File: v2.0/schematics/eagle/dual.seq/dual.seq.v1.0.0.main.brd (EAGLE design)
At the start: 86 x 80 mm, 75 parts, among them IC1 LM324N, IC2 PIC18F2431DIP, IC3 TL084P, IC4 LM324N, IC5 TL082P, J1 RST1, J2 RST2, J3 DIR1, J4 DIR2, J5 CK1, J6 CK2, Q1 20MHz

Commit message: Initial board layout for dual seq main
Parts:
- R1, R10, R11, R12, R13, R14, R15, R16, R17, R18, R19, R2, R20, R21, R22, R23, R24, R25, R26, R27, R28, R29, R3, R30, R31, R32, R33, R4, R5, R6, R7, R8, R9: device _common:0309/10 -> _common:0207/7
- moved LED2 197.7 mm to (88.9, 2.54), turned to 180 degrees
- moved R16 173.8 mm to (85.1, 29.2), turned to 90 degrees
- moved R10 171.5 mm to (87.6, 47.0)
- moved R15 159.1 mm to (82.5, 29.2), turned to 90 degrees
- moved R22 159.1 mm to (69.8, 35.6), turned to 270 degrees
- moved R4 156.0 mm to (64.8, 35.6), turned to 90 degrees
- moved LED1 152.9 mm to (95.9, 2.54), turned to 180 degrees
- moved D3 151.3 mm to (87.6, 44.5)
- moved R3 151.0 mm to (72.4, 35.6), turned to 270 degrees
- moved D5 150.3 mm to (62.2, 15.2), turned to 270 degrees
- moved IC1 149.8 mm to (64.8, 25.4), turned to 180 degrees
- moved R2 141.4 mm to (69.8, 15.2), turned to 270 degrees
- moved R9 137.7 mm to (57.1, 15.2), turned to 270 degrees
- moved D4 133.1 mm to (54.6, 15.2), turned to 270 degrees
- moved R20 132.6 mm to (67.3, 35.6), turned to 270 degrees
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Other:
- board size 86 x 80 mm -> 98.7 x 62.2 mm

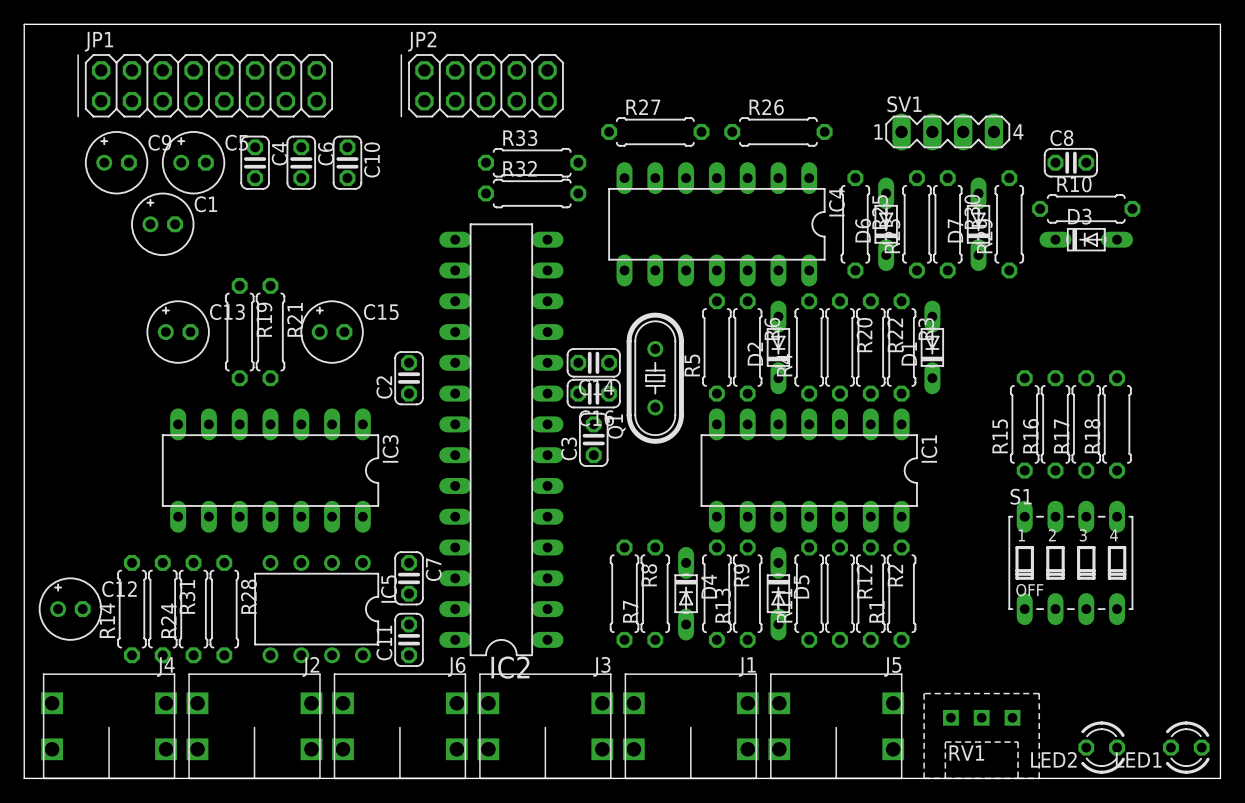
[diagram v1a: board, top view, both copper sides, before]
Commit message: Inital routing for main pnl (too many vias)
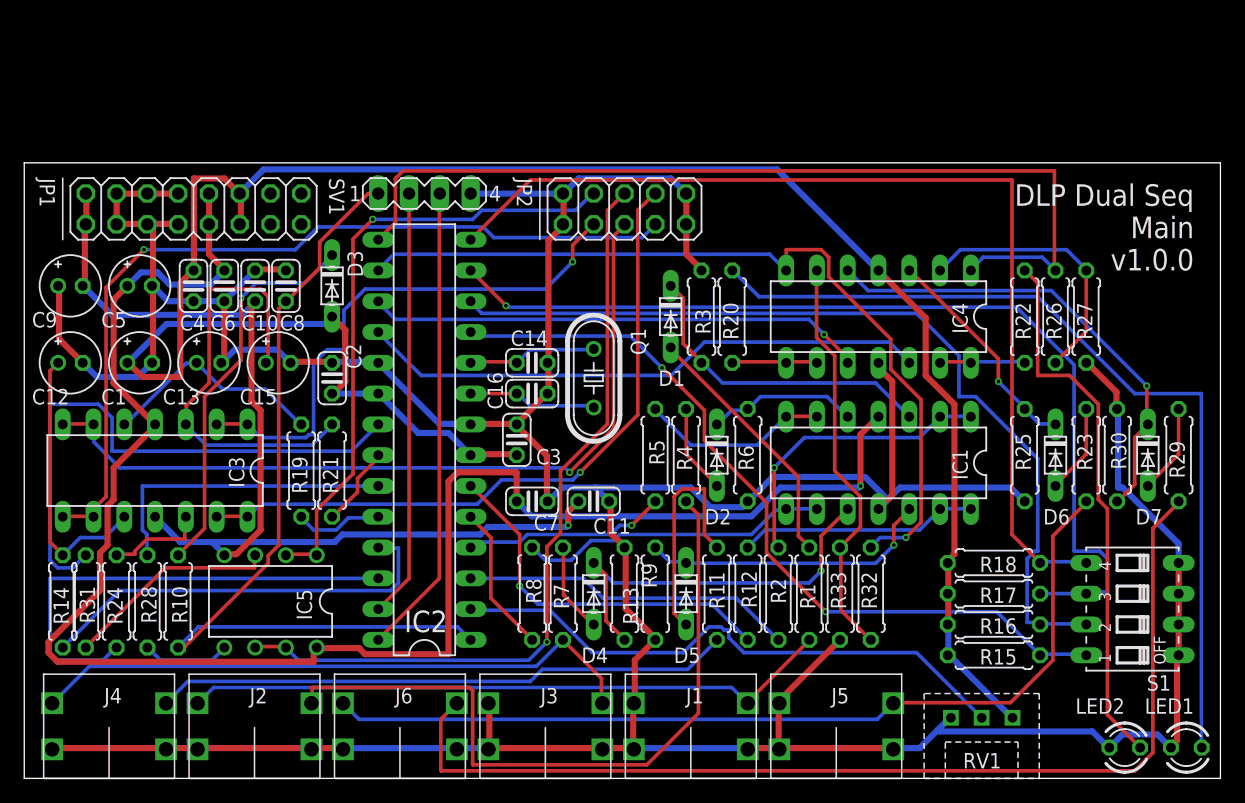
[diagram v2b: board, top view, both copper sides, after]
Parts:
- moved R10 81.6 mm to (12.7, 14.6), turned to 270 degrees
- moved C8 65.6 mm to (21.6, 40.6), turned to 270 degrees
- moved D3 62.3 mm to (25.4, 40.6), turned to 270 degrees
- moved R33 43.7 mm to (67.3, 15.2), turned to 90 degrees
- moved SV1 43.5 mm to (33.0, 48.3)
- moved R32 43.3 mm to (69.8, 15.2), turned to 90 degrees
- moved R27 38.7 mm to (87.6, 38.1), turned to 90 degrees
- moved R26 27.5 mm to (85.1, 38.1), turned to 90 degrees
- moved D6 23.6 mm to (85.1, 26.7), turned to 270 degrees
- moved D7 23.6 mm to (92.7, 26.7), turned to 270 degrees
- moved R23 23.6 mm to (87.6, 26.7)
- moved R25 23.6 mm to (82.5, 26.7), turned to 90 degrees
- moved R29 23.6 mm to (95.2, 26.7)
- moved R30 23.6 mm to (90.2, 26.7)
- moved D1 21.7 mm to (53.3, 38.1), turned to 270 degrees
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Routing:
- net 0V: track 0.00 -> 367.8 mm
- net +5V: track 0.00 -> 171.0 mm
- net +12V: track 0.00 -> 145.5 mm, vias 0 -> 1
- net N$41: track 0.00 -> 87.1 mm
- net -12V: track 0.00 -> 85.9 mm, vias 0 -> 1
- net N$43: track 0.00 -> 83.2 mm
- net N$29: track 0.00 -> 79.9 mm, vias 0 -> 1
- net N$19: track 0.00 -> 76.4 mm
- net N$30: track 0.00 -> 75.4 mm
- net N$28: track 0.00 -> 73.4 mm
- net N$38: track 0.00 -> 72.1 mm
- net VPP: track 0.00 -> 70.4 mm
- net N$21: track 0.00 -> 70.3 mm, vias 0 -> 1
- net N$CV3: track 0.00 -> 70.2 mm, vias 0 -> 1
- net N$CV2: track 0.00 -> 66.6 mm, vias 0 -> 1
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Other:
- board size 98.7 x 62.2 mm -> 98.7 x 50.8 mm
- board text added: "DLP Dual Seq Main v1.0.0"

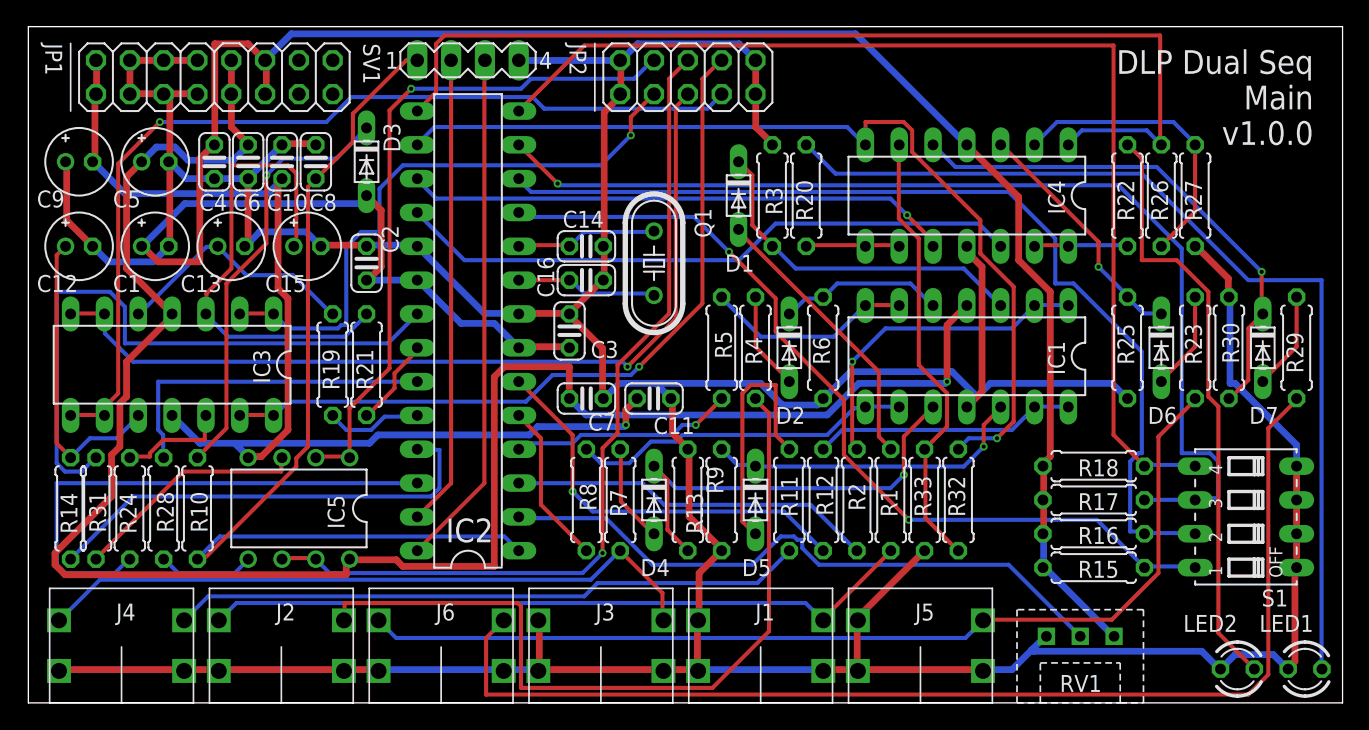
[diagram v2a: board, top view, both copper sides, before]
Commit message: Upated layout and routing for dual.seq main board
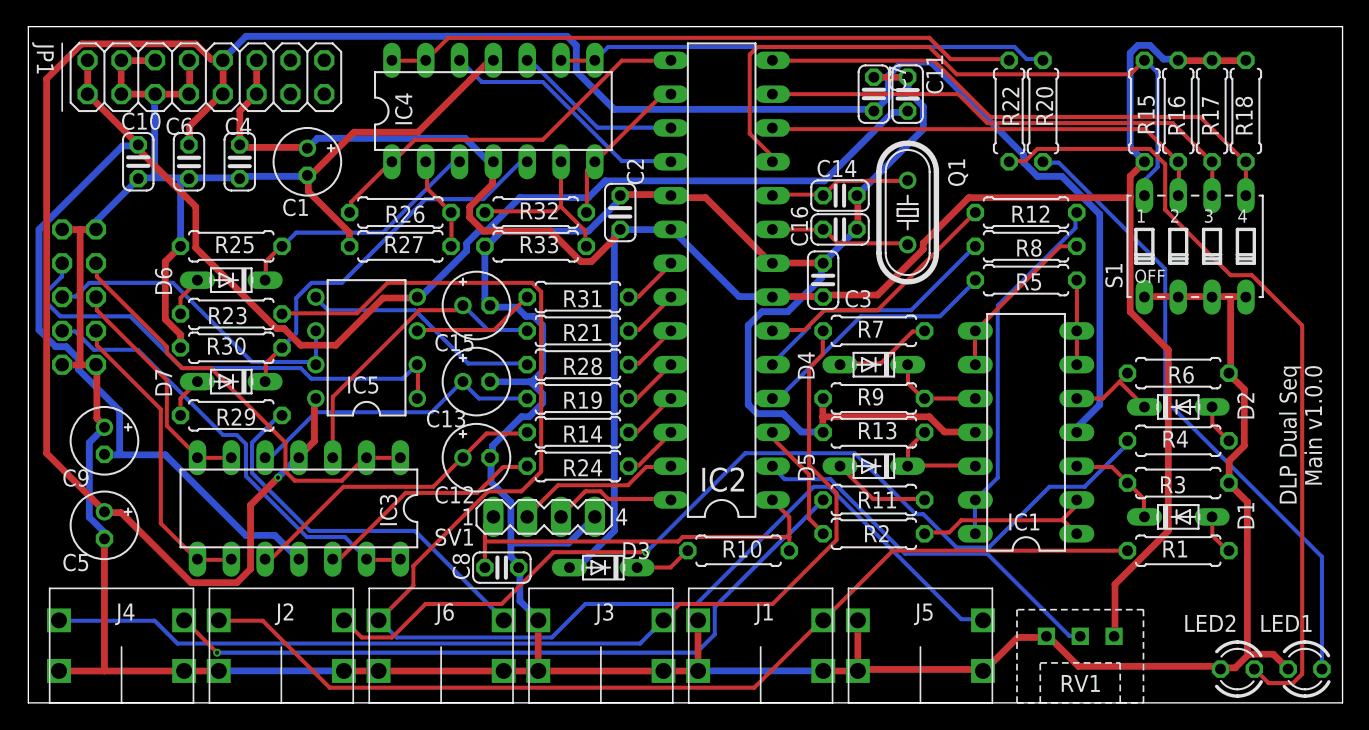
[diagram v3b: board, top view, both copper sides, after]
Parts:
- moved R29 80.2 mm to (15.2, 21.6), turned to 180 degrees
- moved D7 77.5 mm to (15.2, 24.1), turned to 180 degrees
- moved R30 74.9 mm to (15.2, 26.7), turned to 0 degrees
- moved R23 72.4 mm to (15.2, 29.2), turned to 180 degrees
- moved D6 70.0 mm to (15.2, 31.8), turned to 180 degrees
- moved R25 67.7 mm to (15.2, 34.3), turned to 0 degrees
- moved R27 59.8 mm to (27.9, 34.3), turned to 0 degrees
- moved R26 57.2 mm to (27.9, 36.8), turned to 180 degrees
- moved JP2 48.6 mm to (3.81, 30.5), flipped to the bottom, turned to 270 degrees
- moved D1 40.9 mm to (86.4, 14.0), turned to 0 degrees
- moved R10 40.8 mm to (53.3, 11.4), turned to 0 degrees
- moved R31 39.5 mm to (41.3, 30.5), turned to 180 degrees
- moved R14 38.5 mm to (41.3, 20.3), turned to 180 degrees
- moved R32 38.4 mm to (38.1, 36.8), turned to 0 degrees
- moved R8 38.1 mm to (74.9, 34.3), turned to 180 degrees
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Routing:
- net N$21: track 70.3 -> 11.9 mm, vias 1 -> 0
- net N$41: track 87.1 -> 28.9 mm
- net N$CV2: track 66.6 -> 17.8 mm, vias 1 -> 0
- net N$CV3: track 70.2 -> 22.9 mm, vias 1 -> 0
- net N$19: track 76.4 -> 29.2 mm
- net -12V: track 85.9 -> 129.6 mm, vias 1 -> 0
- net N$10: track 47.7 -> 4.26 mm
- net N$29: track 79.9 -> 37.7 mm, vias 1 -> 0
- net N$43: track 83.2 -> 41.3 mm
- net N$34: track 7.18 -> 47.8 mm
- net N$GATE2: track 64.9 -> 24.6 mm, vias 1 -> 0
- net N$28: track 73.4 -> 34.1 mm
- net VPP: track 70.4 -> 31.4 mm
- net N$8: track 39.4 -> 4.25 mm
- net +12V: track 145.5 -> 179.8 mm
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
